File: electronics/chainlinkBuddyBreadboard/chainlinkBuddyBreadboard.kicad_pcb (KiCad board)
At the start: 2 copper layers, 33 x 19 mm, 2 parts, among them J1 Output, J2 Conn_01x05_Male

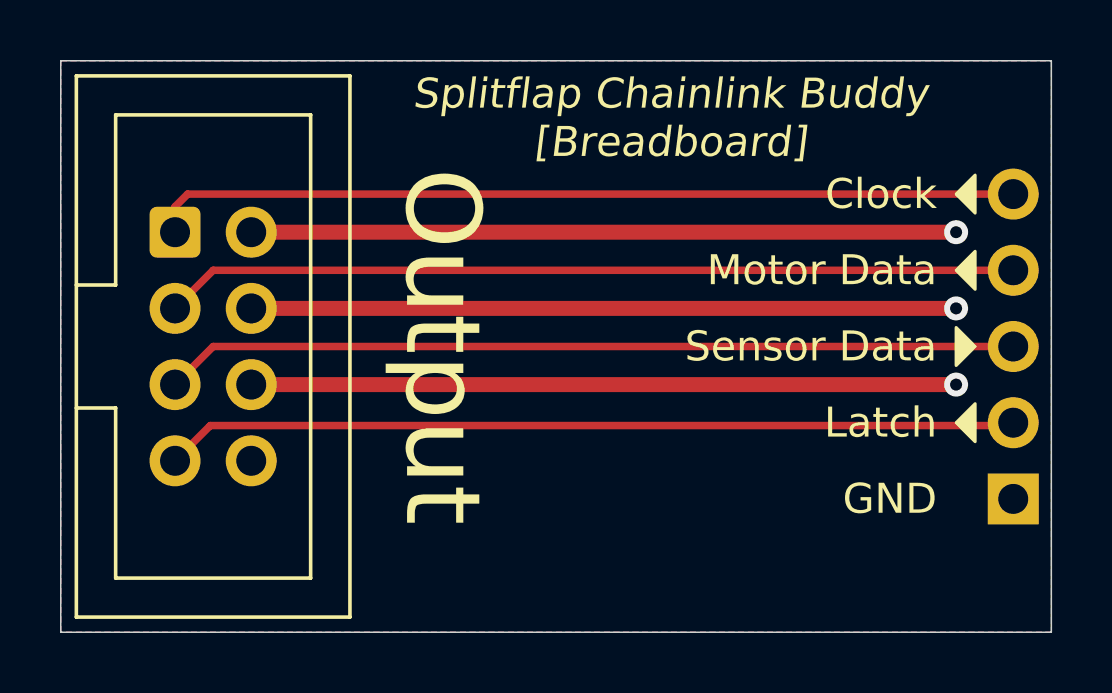
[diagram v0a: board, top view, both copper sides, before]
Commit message: Add version numbers to chainlink PCBs
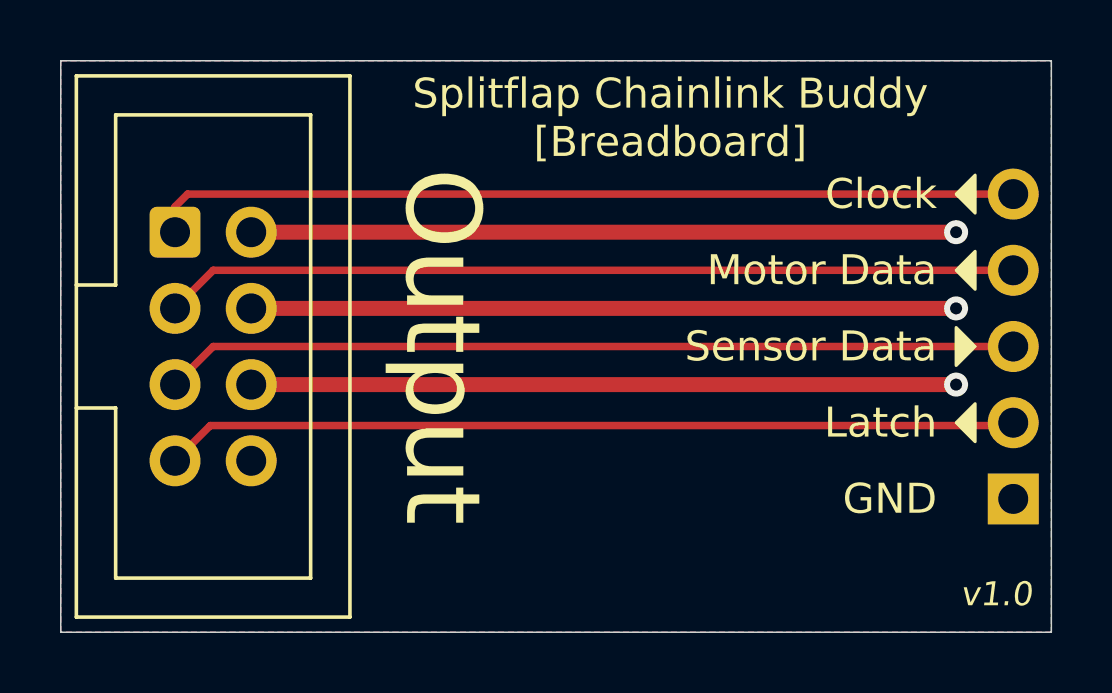
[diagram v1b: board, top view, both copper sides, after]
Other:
- board text added: "v1.0"
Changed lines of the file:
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@@
   (general
     (thickness 1.6)
-    (drawings 27)
+    (drawings 28)
     (tracks 16)
     (zones 0)
@@
   )
   (setup
-    (last_trace_width 0.5)
+    (last_trace_width 0.25)
     (user_trace_width 0.25)
     (user_trace_width 0.5)
@@
       (effects (font (size 1 1) (thickness 0.15)) (justify mirror))
     )
-    (fp_text user %R (at 0 -5.08 -90) (layer B.Fab)
-      (effects (font (size 1 1) (thickness 0.15)) (justify mirror))
-    )
     (fp_line (start 1.8 1.8) (end -1.8 1.8) (layer B.CrtYd) (width 0.05))
     (fp_line (start 1.8 -11.95) (end 1.8 1.8) (layer B.CrtYd) (width 0.05))
@@
     (fp_line (start 1.27 1.27) (end 1.27 -11.43) (layer B.Fab) (width 0.1))
     (fp_line (start -0.635 1.27) (end 1.27 1.27) (layer B.Fab) (width 0.1))
+    (fp_text user %R (at 0 -5.08 -90) (layer B.Fab)
+      (effects (font (size 1 1) (thickness 0.15)) (justify mirror))
+    )
     (pad 5 thru_hole oval (at 0 -10.16) (size 1.7 1.7) (drill 1) (layers *.Cu *.Mask)
       (net 5 /CLOCK))
@@
     )
   )
+  (gr_text v1.0 (at 95.885 81.28) (layer F.SilkS)
+    (effects (font (size 0.8 0.8) (thickness 0.09) italic) (justify right))
+  )
   (dimension 19.05 (width 0.15) (layer Cmts.User)
     (gr_text "19.050 mm" (at 59.660001 73.025 270) (layer Cmts.User)
@@
   )
   (gr_text "Splitflap Chainlink Buddy\n[Breadboard]" (at 83.82 65.405) (layer F.SilkS)
-    (effects (font (size 1 1) (thickness 0.1) italic))
+    (effects (font (size 1 1) (thickness 0.12)))
   )
   (gr_line (start 63.5 82.55) (end 63.5 63.5) (layer Edge.Cuts) (width 0.05))

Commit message: Add more ground vias to Chainlink Buddy Breadboard
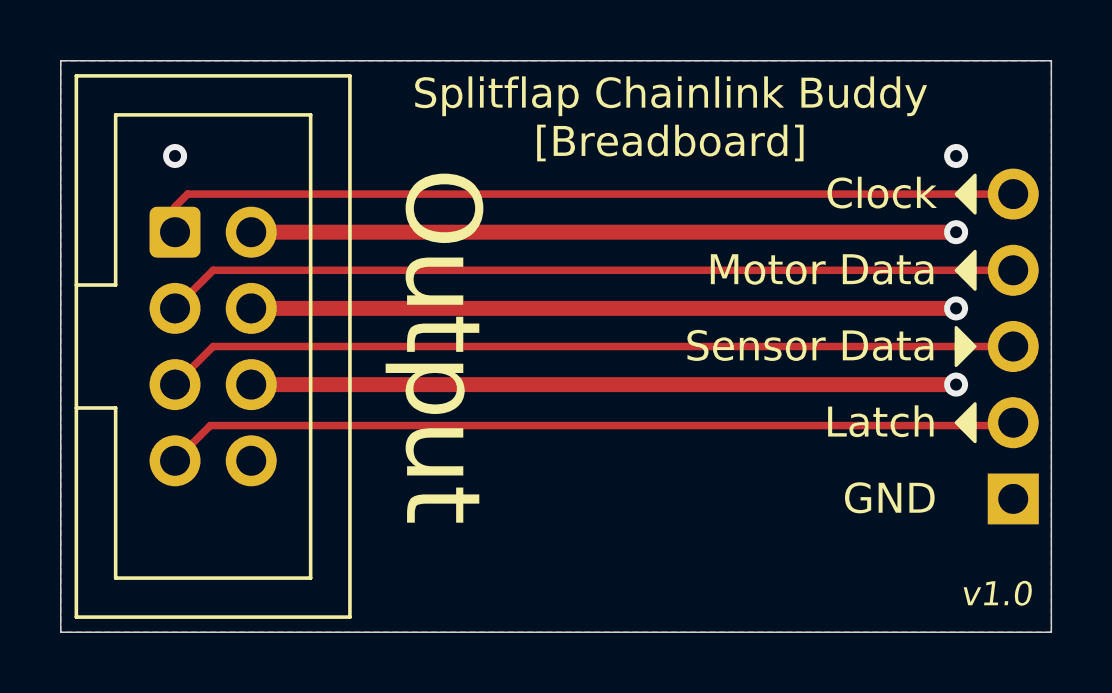
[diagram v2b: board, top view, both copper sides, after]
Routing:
- net GND: vias 3 -> 5
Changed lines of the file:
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@@
     (thickness 1.6)
     (drawings 28)
-    (tracks 16)
+    (tracks 18)
     (zones 0)
     (modules 2)
@@
       (effects (font (size 1 1) (thickness 0.15)) (justify mirror))
     )
+    (fp_line (start -0.635 1.27) (end 1.27 1.27) (layer B.Fab) (width 0.1))
+    (fp_line (start 1.27 1.27) (end 1.27 -11.43) (layer B.Fab) (width 0.1))
+    (fp_line (start 1.27 -11.43) (end -1.27 -11.43) (layer B.Fab) (width 0.1))
+    (fp_line (start -1.27 -11.43) (end -1.27 0.635) (layer B.Fab) (width 0.1))
+    (fp_line (start -1.27 0.635) (end -0.635 1.27) (layer B.Fab) (width 0.1))
+    (fp_line (start -1.8 1.8) (end -1.8 -11.95) (layer B.CrtYd) (width 0.05))
+    (fp_line (start -1.8 -11.95) (end 1.8 -11.95) (layer B.CrtYd) (width 0.05))
+    (fp_line (start 1.8 -11.95) (end 1.8 1.8) (layer B.CrtYd) (width 0.05))
     (fp_line (start 1.8 1.8) (end -1.8 1.8) (layer B.CrtYd) (width 0.05))
-    (fp_line (start 1.8 -11.95) (end 1.8 1.8) (layer B.CrtYd) (width 0.05))
-    (fp_line (start -1.8 -11.95) (end 1.8 -11.95) (layer B.CrtYd) (width 0.05))
-    (fp_line (start -1.8 1.8) (end -1.8 -11.95) (layer B.CrtYd) (width 0.05))
-    (fp_line (start -1.27 0.635) (end -0.635 1.27) (layer B.Fab) (width 0.1))
-    (fp_line (start -1.27 -11.43) (end -1.27 0.635) (layer B.Fab) (width 0.1))
-    (fp_line (start 1.27 -11.43) (end -1.27 -11.43) (layer B.Fab) (width 0.1))
-    (fp_line (start 1.27 1.27) (end 1.27 -11.43) (layer B.Fab) (width 0.1))
-    (fp_line (start -0.635 1.27) (end 1.27 1.27) (layer B.Fab) (width 0.1))
     (fp_text user %R (at 0 -5.08 -90) (layer B.Fab)
       (effects (font (size 1 1) (thickness 0.15)) (justify mirror))
@@
       (effects (font (size 1 1) (thickness 0.15)))
     )
+    (fp_line (start -3.18 -4.1) (end -2.18 -5.1) (layer F.Fab) (width 0.1))
+    (fp_line (start -2.18 -5.1) (end 5.72 -5.1) (layer F.Fab) (width 0.1))
+    (fp_line (start 5.72 -5.1) (end 5.72 12.72) (layer F.Fab) (width 0.1))
+    (fp_line (start 5.72 12.72) (end -3.18 12.72) (layer F.Fab) (width 0.1))
+    (fp_line (start -3.18 12.72) (end -3.18 -4.1) (layer F.Fab) (width 0.1))
+    (fp_line (start -3.18 1.76) (end -1.98 1.76) (layer F.Fab) (width 0.1))
+    (fp_line (start -1.98 1.76) (end -1.98 -3.91) (layer F.Fab) (width 0.1))
+    (fp_line (start -1.98 -3.91) (end 4.52 -3.91) (layer F.Fab) (width 0.1))
+    (fp_line (start 4.52 -3.91) (end 4.52 11.53) (layer F.Fab) (width 0.1))
+    (fp_line (start 4.52 11.53) (end -1.98 11.53) (layer F.Fab) (width 0.1))
+    (fp_line (start -1.98 11.53) (end -1.98 5.86) (layer F.Fab) (width 0.1))
+    (fp_line (start -1.98 5.86) (end -1.98 5.86) (layer F.Fab) (width 0.1))
+    (fp_line (start -1.98 5.86) (end -3.18 5.86) (layer F.Fab) (width 0.1))
+    (fp_line (start -3.29 -5.21) (end 5.83 -5.21) (layer F.SilkS) (width 0.12))
+    (fp_line (start 5.83 -5.21) (end 5.83 12.83) (layer F.SilkS) (width 0.12))
+    (fp_line (start 5.83 12.83) (end -3.29 12.83) (layer F.SilkS) (width 0.12))
+    (fp_line (start -3.29 12.83) (end -3.29 -5.21) (layer F.SilkS) (width 0.12))
+    (fp_line (start -3.29 1.76) (end -1.98 1.76) (layer F.SilkS) (width 0.12))
+    (fp_line (start -1.98 1.76) (end -1.98 -3.91) (layer F.SilkS) (width 0.12))
+    (fp_line (start -1.98 -3.91) (end 4.52 -3.91) (layer F.SilkS) (width 0.12))
+    (fp_line (start 4.52 -3.91) (end 4.52 11.53) (layer F.SilkS) (width 0.12))
+    (fp_line (start 4.52 11.53) (end -1.98 11.53) (layer F.SilkS) (width 0.12))
+    (fp_line (start -1.98 11.53) (end -1.98 5.86) (layer F.SilkS) (width 0.12))
+    (fp_line (start -1.98 5.86) (end -1.98 5.86) (layer F.SilkS) (width 0.12))
+    (fp_line (start -1.98 5.86) (end -3.29 5.86) (layer F.SilkS) (width 0.12))
+    (fp_line (start -3.68 -5.6) (end -3.68 13.22) (layer F.CrtYd) (width 0.05))
+    (fp_line (start -3.68 13.22) (end 6.22 13.22) (layer F.CrtYd) (width 0.05))
+    (fp_line (start 6.22 13.22) (end 6.22 -5.6) (layer F.CrtYd) (width 0.05))
     (fp_line (start 6.22 -5.6) (end -3.68 -5.6) (layer F.CrtYd) (width 0.05))
-    (fp_line (start 6.22 13.22) (end 6.22 -5.6) (layer F.CrtYd) (width 0.05))
-    (fp_line (start -3.68 13.22) (end 6.22 13.22) (layer F.CrtYd) (width 0.05))
-    (fp_line (start -3.68 -5.6) (end -3.68 13.22) (layer F.CrtYd) (width 0.05))
-    (fp_line (start -1.98 5.86) (end -3.29 5.86) (layer F.SilkS) (width 0.12))
-    (fp_line (start -1.98 5.86) (end -1.98 5.86) (layer F.SilkS) (width 0.12))
-    (fp_line (start -1.98 11.53) (end -1.98 5.86) (layer F.SilkS) (width 0.12))
-    (fp_line (start 4.52 11.53) (end -1.98 11.53) (layer F.SilkS) (width 0.12))
-    (fp_line (start 4.52 -3.91) (end 4.52 11.53) (layer F.SilkS) (width 0.12))
-    (fp_line (start -1.98 -3.91) (end 4.52 -3.91) (layer F.SilkS) (width 0.12))
-    (fp_line (start -1.98 1.76) (end -1.98 -3.91) (layer F.SilkS) (width 0.12))
-    (fp_line (start -3.29 1.76) (end -1.98 1.76) (layer F.SilkS) (width 0.12))
-    (fp_line (start -3.29 12.83) (end -3.29 -5.21) (layer F.SilkS) (width 0.12))
-    (fp_line (start 5.83 12.83) (end -3.29 12.83) (layer F.SilkS) (width 0.12))
-    (fp_line (start 5.83 -5.21) (end 5.83 12.83) (layer F.SilkS) (width 0.12))
-    (fp_line (start -3.29 -5.21) (end 5.83 -5.21) (layer F.SilkS) (width 0.12))
-    (fp_line (start -1.98 5.86) (end -3.18 5.86) (layer F.Fab) (width 0.1))
-    (fp_line (start -1.98 5.86) (end -1.98 5.86) (layer F.Fab) (width 0.1))
-    (fp_line (start -1.98 11.53) (end -1.98 5.86) (layer F.Fab) (width 0.1))
-    (fp_line (start 4.52 11.53) (end -1.98 11.53) (layer F.Fab) (width 0.1))
-    (fp_line (start 4.52 -3.91) (end 4.52 11.53) (layer F.Fab) (width 0.1))
-    (fp_line (start -1.98 -3.91) (end 4.52 -3.91) (layer F.Fab) (width 0.1))
-    (fp_line (start -1.98 1.76) (end -1.98 -3.91) (layer F.Fab) (width 0.1))
-    (fp_line (start -3.18 1.76) (end -1.98 1.76) (layer F.Fab) (width 0.1))
-    (fp_line (start -3.18 12.72) (end -3.18 -4.1) (layer F.Fab) (width 0.1))
-    (fp_line (start 5.72 12.72) (end -3.18 12.72) (layer F.Fab) (width 0.1))
-    (fp_line (start 5.72 -5.1) (end 5.72 12.72) (layer F.Fab) (width 0.1))
-    (fp_line (start -2.18 -5.1) (end 5.72 -5.1) (layer F.Fab) (width 0.1))
-    (fp_line (start -3.18 -4.1) (end -2.18 -5.1) (layer F.Fab) (width 0.1))
     (fp_text user %R (at 1.27 3.81 90) (layer F.Fab)
       (effects (font (size 1 1) (thickness 0.15)))
@@
   (segment (start 93.345 71.755) (end 69.85 71.755) (width 0.5) (layer F.Cu) (net 1))
   (segment (start 69.85 74.295) (end 93.345 74.295) (width 0.5) (layer F.Cu) (net 1))
+  (via (at 67.31 66.675) (size 0.8) (drill 0.4) (layers F.Cu B.Cu) (net 1))
+  (via (at 93.345 66.675) (size 0.8) (drill 0.4) (layers F.Cu B.Cu) (net 1))
   (segment (start 95.155001 75.659999) (end 95.25 75.565) (width 0.25) (layer F.Cu) (net 2))
   (segment (start 68.485001 75.659999) (end 95.155001 75.659999) (width 0.25) (layer F.Cu) (net 2))
